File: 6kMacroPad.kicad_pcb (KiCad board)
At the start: 2 copper layers, 88.9 x 48.3 mm, 29 parts, among them J1 USB, K1 klack, K2 klack, K3 klack, K4 klack, K5 klack, K6 klack, U1 ATMEGA32U4, Y1 XTAL

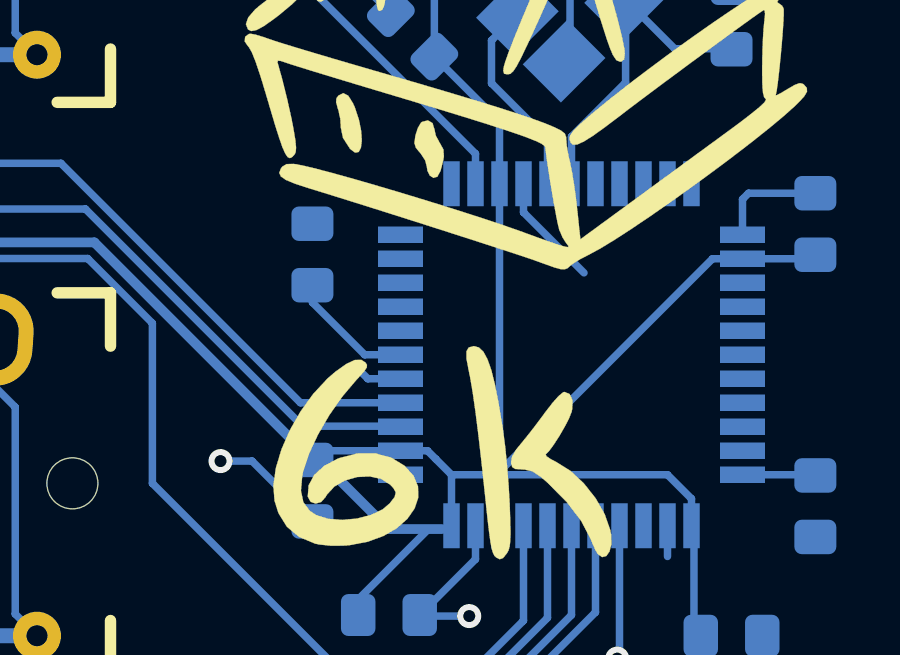
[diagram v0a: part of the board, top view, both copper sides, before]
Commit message: Fixed Vbus not connected, added pics
- now Vbus is connected to VCC
- added more pics of the build
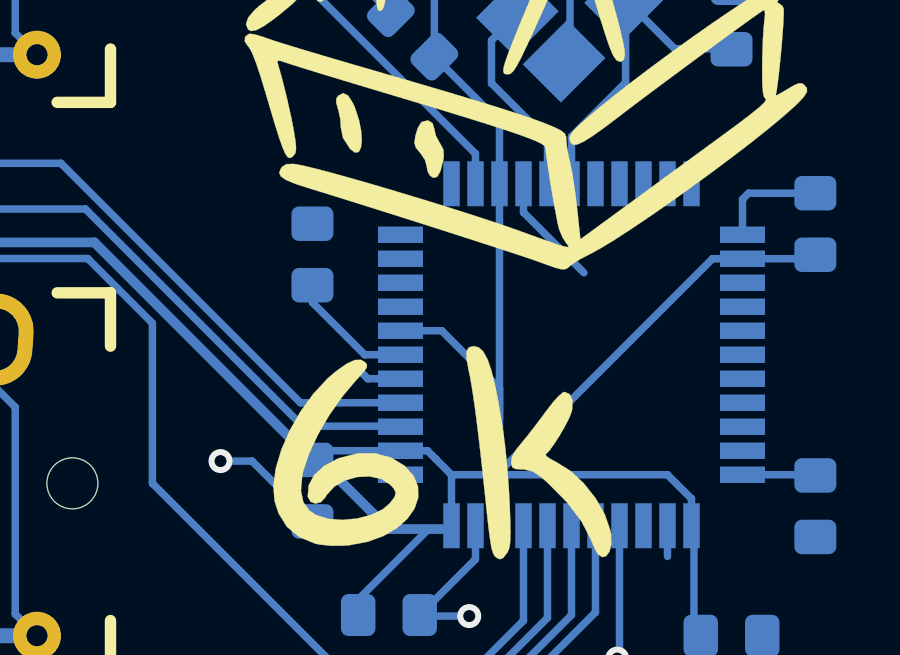
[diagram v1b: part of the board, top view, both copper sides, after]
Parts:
- J1: value USB -> USB_mini_micro_B
- K1, K2, K3, K4, K5, K6: value klack -> KEYSW
- SW1: renamed from RESET; value RESET_SW -> SW_PUSH
- Y1: value XTAL -> Crystal_GND24
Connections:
- U1 pad 7: Net-(U1-Pad7) -> VCC
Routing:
- net VCC: track 133.3 -> 138.4 mm
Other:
- board text added: "6K Macro Pad rev 1.1"
- board text removed: "6K Macro Pad"
